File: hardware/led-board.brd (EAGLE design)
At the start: 100 x 15.3 mm, 22 parts, among them U1 ATMEGA168PA-AU

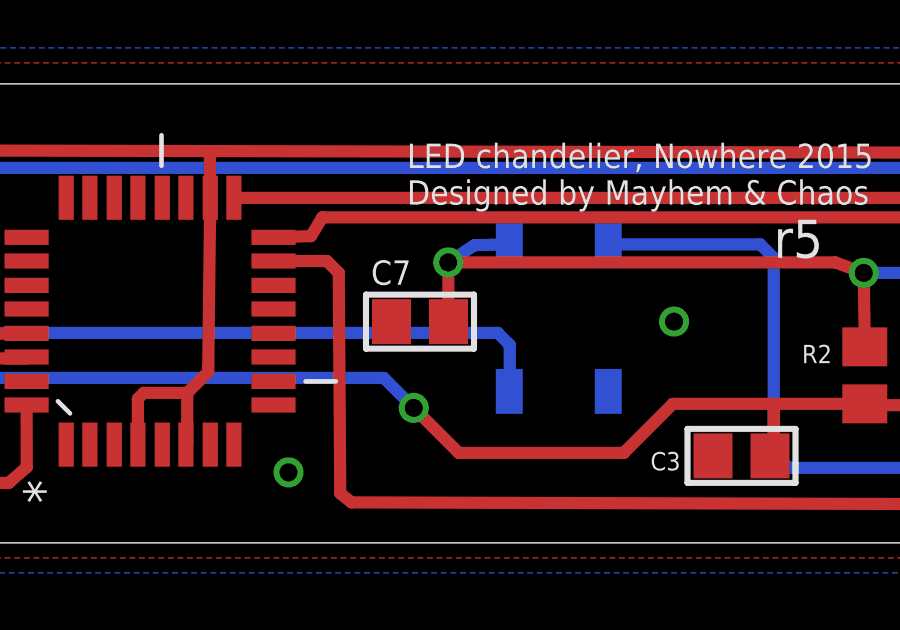
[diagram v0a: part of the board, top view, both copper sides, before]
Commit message: Moved C7 further away from U1
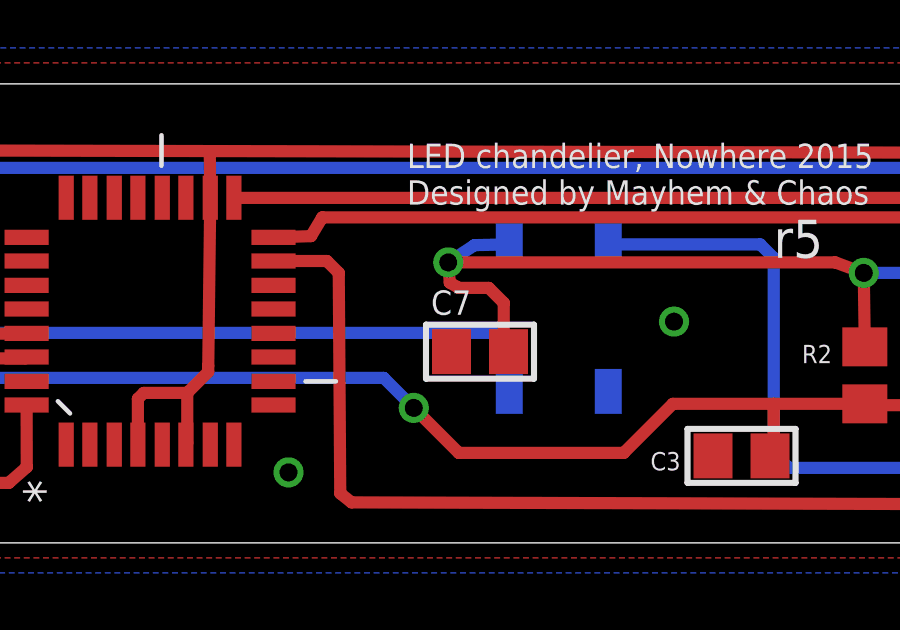
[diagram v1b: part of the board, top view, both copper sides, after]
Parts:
- moved C7 2.24 mm to (62.7, 6.38)
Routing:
- net VCC: track 183.6 -> 186.1 mm
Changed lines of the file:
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@@
 <attribute name="MPN" value="MCSH21B104K250CT" x="39.12" y="7.48" size="1.778" layer="27" rot="R270" display="off"/>
 </element>
-<element name="C7" library="microbuilder" package="0805" value="100nF" x="60.708" y="7.375" smashed="yes" rot="R180">
-<attribute name="NAME" x="59.076" y="8.602" size="0.8128" layer="25" ratio="18"/>
-<attribute name="OC_NEWARK" value="23T7445" x="60.708" y="7.375" size="1.778" layer="27" rot="R180" display="off"/>
-<attribute name="MF" value="" x="60.708" y="7.375" size="1.778" layer="27" rot="R180" display="off"/>
-<attribute name="MPN" value="MCSH21B104K250CT" x="60.708" y="7.375" size="1.778" layer="27" rot="R180" display="off"/>
+<element name="C7" library="microbuilder" package="0805" value="100nF" x="62.708" y="6.375" smashed="yes" rot="R180">
+<attribute name="NAME" x="61.076" y="7.602" size="0.8128" layer="25" ratio="18"/>
+<attribute name="OC_NEWARK" value="23T7445" x="62.708" y="6.375" size="1.778" layer="27" rot="R180" display="off"/>
+<attribute name="MF" value="" x="62.708" y="6.375" size="1.778" layer="27" rot="R180" display="off"/>
+<attribute name="MPN" value="MCSH21B104K250CT" x="62.708" y="6.375" size="1.778" layer="27" rot="R180" display="off"/>
 </element>
 <element name="C8" library="microbuilder" package="0805" value="100nF" x="90.92" y="8.58" smashed="yes" rot="R90">
@@
 <wire x1="85.075" y1="9.7" x2="85.55" y2="9.225" width="0.4064" layer="1"/>
 <wire x1="85.55" y1="9.225" x2="85.55" y2="8.4" width="0.4064" layer="1"/>
-<wire x1="61.658" y1="7.375" x2="61.65" y2="9.35" width="0.4064" layer="1"/>
 <via x="61.65" y="9.35" extent="1-16" drill="0.6"/>
 <wire x1="61.65" y1="9.35" x2="62.525" y2="9.925" width="0.4064" layer="16"/>
@@
 <wire x1="61.65" y1="9.35" x2="74.55" y2="9.35" width="0.4064" layer="1"/>
 <wire x1="74.55" y1="9.35" x2="75.5" y2="9" width="0.4064" layer="1"/>
+<wire x1="63.658" y1="6.375" x2="63.5" y2="6.375" width="0.4064" layer="1"/>
+<wire x1="63.5" y1="6.375" x2="63.5" y2="8" width="0.4064" layer="1"/>
+<wire x1="63.5" y1="8" x2="63" y2="8.5" width="0.4064" layer="1"/>
+<wire x1="63" y1="8.5" x2="62" y2="8.5" width="0.4064" layer="1"/>
+<wire x1="62" y1="8.5" x2="61.7" y2="8.675" width="0.4064" layer="1"/>
+<wire x1="61.7" y1="8.675" x2="61.65" y2="9.35" width="0.4064" layer="1"/>
 </signal>
 <signal name="LED">

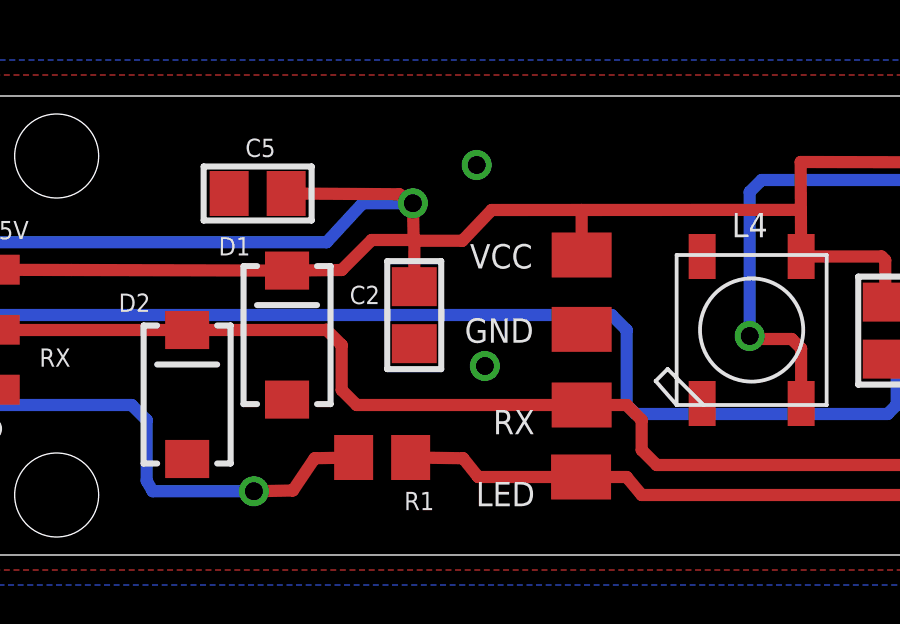
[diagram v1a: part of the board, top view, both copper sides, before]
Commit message: Increased bulk capacitance (C1) to 47uF.
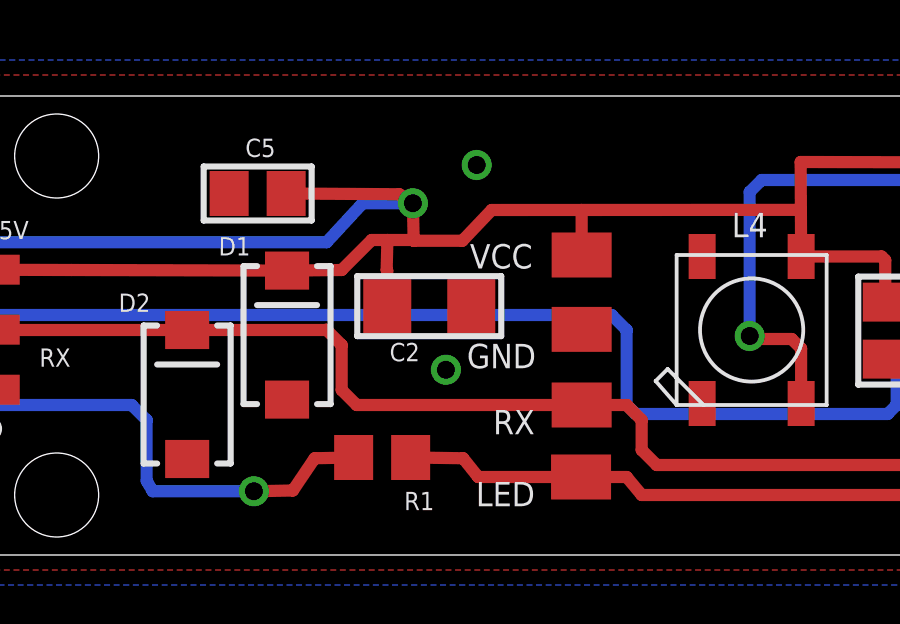
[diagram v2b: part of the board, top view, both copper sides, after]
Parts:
- C2: value 1uF -> 47uF; device microbuilder:0805 -> microbuilder:1206
- moved C2 0.58 mm to (23.9, 8.29), turned to 0 degrees
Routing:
- net VCC: track 186.1 -> 186.8 mm
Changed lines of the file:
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@@
 <wire x1="100" y1="15.3" x2="0" y2="15.3" width="0" layer="20"/>
 <wire x1="0" y1="15.3" x2="0" y2="0" width="0" layer="20"/>
-<text x="25.1" y="7.075" size="0.8128" layer="25">GND</text>
+<text x="25.175" y="6.225" size="0.8128" layer="25">GND</text>
 <text x="26.05" y="4.025" size="0.8128" layer="25">RX</text>
 <text x="25.475" y="1.625" size="0.8128" layer="25">LED</text>
@@
 <attribute name="MPN" value="MCSH21B104K250CT" x="43.02" y="10.98" size="1.778" layer="27" rot="R180" display="off"/>
 </element>
-<element name="C2" library="microbuilder" package="0805" value="1uF" x="23.42" y="7.995" smashed="yes" rot="R270">
-<attribute name="NAME" x="21.268" y="8.363" size="0.6096" layer="25" ratio="18"/>
-<attribute name="OC_NEWARK" value="68R4880" x="23.42" y="7.995" size="1.778" layer="27" rot="R270" display="off"/>
-<attribute name="MF" value="" x="23.42" y="7.995" size="1.778" layer="27" rot="R270" display="off"/>
-<attribute name="MPN" value="CC0805KKX7R7BB105" x="23.42" y="7.995" size="1.778" layer="27" rot="R270" display="off"/>
+<element name="C2" library="microbuilder" package="1206" value="47uF" x="23.92" y="8.295" smashed="yes">
+<attribute name="NAME" x="23.602" y="7.068" size="0.6096" layer="25" ratio="18" rot="R180"/>
+<attribute name="OC_NEWARK" value="68R4880" x="23.92" y="8.295" size="1.778" layer="27" display="off"/>
+<attribute name="MF" value="" x="23.92" y="8.295" size="1.778" layer="27" display="off"/>
+<attribute name="MPN" value="CC0805KKX7R7BB105" x="23.92" y="8.295" size="1.778" layer="27" display="off"/>
 </element>
 <element name="C5" library="microbuilder" package="0805" value="100nF" x="18.2" y="12.05" smashed="yes" rot="R180">
@@
 <contactref element="U1" pad="21"/>
 <contactref element="C3" pad="2"/>
-<via x="25.775" y="6.3" extent="1-16" drill="0.6"/>
+<via x="24.475" y="6.175" extent="1-16" drill="0.6"/>
 <contactref element="D2" pad="A"/>
 <contactref element="D1" pad="A"/>
@@
 <wire x1="19.18" y1="9.48" x2="21" y2="9.5" width="0.4064" layer="1"/>
 <wire x1="21" y1="9.5" x2="22" y2="10.5" width="0.4064" layer="1"/>
-<wire x1="22" y1="10.5" x2="23.425" y2="10.5" width="0.4064" layer="1"/>
+<wire x1="22" y1="10.5" x2="22.525" y2="10.5" width="0.4064" layer="1"/>
+<wire x1="22.525" y1="10.5" x2="23.425" y2="10.5" width="0.4064" layer="1"/>
 <wire x1="23.425" y1="10.5" x2="23.4" y2="10.475" width="0.4064" layer="1"/>
 <wire x1="23.4" y1="10.475" x2="25.025" y2="10.475" width="0.4064" layer="1"/>
 <wire x1="25.025" y1="10.475" x2="26" y2="11.5" width="0.4064" layer="1"/>
-<wire x1="23.42" y1="8.945" x2="23.425" y2="10.5" width="0.4064" layer="1"/>
 <wire x1="26" y1="11.5" x2="28.9998" y2="11.50119375" width="0.4064" layer="1"/>
 <wire x1="28.9998" y1="11.50119375" x2="36.30810625" y2="11.504103125" width="0.4064" layer="1"/>
@@
 <wire x1="62" y1="8.5" x2="61.7" y2="8.675" width="0.4064" layer="1"/>
 <wire x1="61.7" y1="8.675" x2="61.65" y2="9.35" width="0.4064" layer="1"/>
+<wire x1="22.52" y1="8.295" x2="22.52" y2="9.48" width="0.4064" layer="1"/>
+<wire x1="22.52" y1="9.48" x2="22.5" y2="9.5" width="0.4064" layer="1"/>
+<wire x1="22.5" y1="9.5" x2="22.525" y2="10.5" width="0.4064" layer="1"/>
 </signal>
 <signal name="LED">

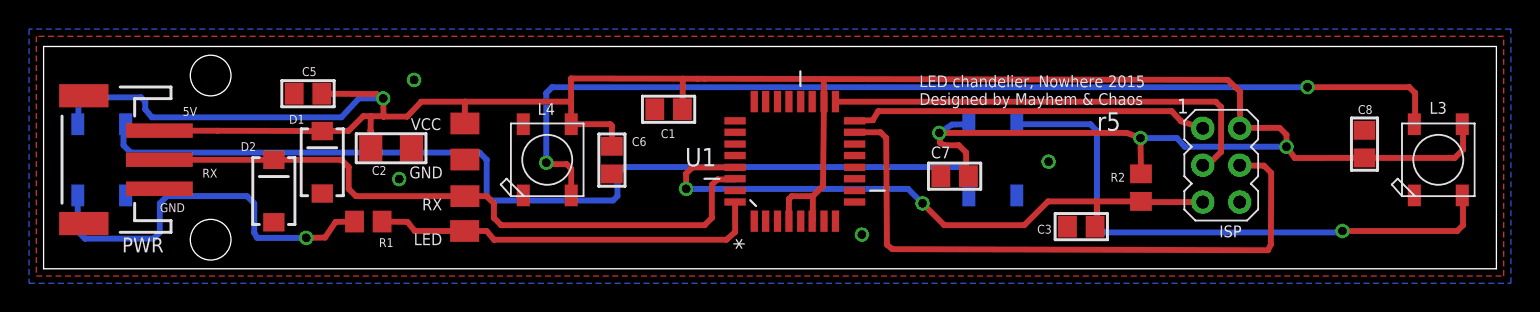
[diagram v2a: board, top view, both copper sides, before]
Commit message: Changed L# -> D# for the LEDs
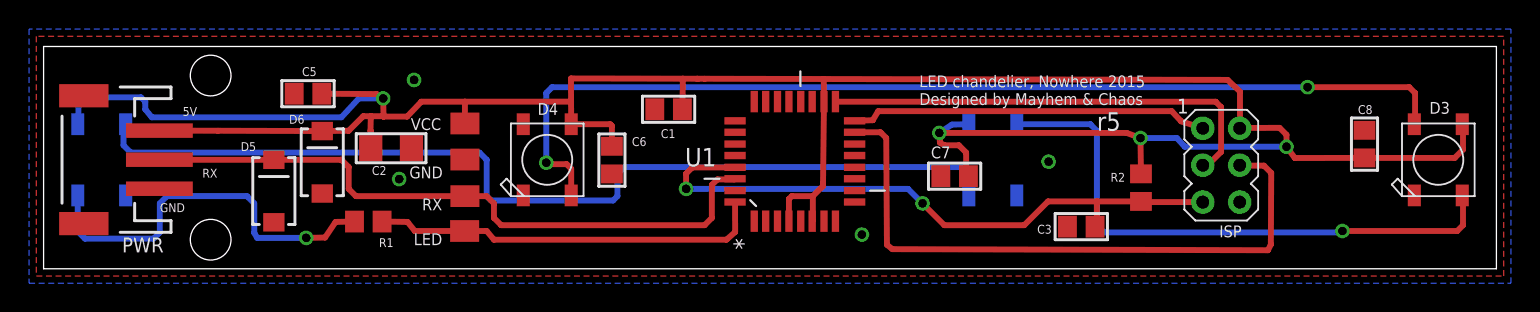
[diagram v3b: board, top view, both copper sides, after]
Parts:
- removed L1, L2: WS2812B, adafruit:WS2812B
- added D5, D6: BA340A, SparkFun-DiscreteSemi:SMA-DIODE
- D1, D2: value BA340A -> WS2812B; device SparkFun-DiscreteSemi:SMA-DIODE -> adafruit:WS2812B
- moved D2 49.5 mm to (65.3, 7.50), flipped to the bottom
- moved D1 15.2 mm to (4.00, 7.50), flipped to the bottom
- renumbered L3 to D3, L4 to D4
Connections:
- removed net N$5: D3.4-DIN, L2.2-DOUT
- new net D3: D2.2-DOUT, D3.4-DIN
- net GND: now also D1.3-GND, D2.3-GND, D5.A, D6.A; no longer D1.A, D2.A, L1.3-GND, L2.3-GND
- net N$2: now also D1.2-DOUT, D2.4-DIN; no longer L1.2-DOUT, L2.4-DIN
- net N$8: now also D1.4-DIN; no longer L1.4-DIN
- net RX: now also D5.C; no longer D2.C
- net VCC: now also D1.1-VDD, D2.1-VDD, D6.C; no longer D1.C, L1.1-VDD, L2.1-VDD
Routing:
- net N$5: track 39.9 -> 0.00 mm, vias 1 -> 0
- net D3: track 0.00 -> 39.9 mm, vias 0 -> 1
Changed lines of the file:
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@@
 <attribute name="MPN" value="MCSH21B104K250CT" x="90.92" y="8.58" size="1.778" layer="27" rot="R90" display="off"/>
 </element>
-<element name="D1" library="SparkFun-DiscreteSemi" package="SMA-DIODE" value="BA340A" x="19.18" y="7.33" smashed="yes" rot="R90">
+<element name="D6" library="SparkFun-DiscreteSemi" package="SMA-DIODE" value="BA340A" x="19.18" y="7.33" smashed="yes" rot="R90">
 <attribute name="PROD_ID" value="DIO-09886" x="19.18" y="7.33" size="1.778" layer="27" rot="R90" display="off"/>
 <attribute name="NAME" x="17.954" y="10.594" size="0.6096" layer="25" rot="R180"/>
@@
 <attribute name="MPN" value="" x="81.06" y="7.13" size="1.778" layer="27" display="off"/>
 </element>
-<element name="L1" library="adafruit" package="WS2812B" value="WS2812B" x="4" y="7.5" smashed="yes" rot="MR90">
+<element name="D1" library="adafruit" package="WS2812B" value="WS2812B" x="4" y="7.5" smashed="yes" rot="MR90">
 <attribute name="NAME" x="4.5125" y="10.3425" size="0.8128" layer="26" ratio="10" rot="MR0"/>
 <attribute name="OC_NEWARK" value="43Y4720" x="4" y="7.5" size="1.778" layer="28" rot="MR90" display="off"/>
@@
 <attribute name="MPN" value="WS2812B" x="4" y="7.5" size="1.778" layer="28" rot="MR90" display="off"/>
 </element>
-<element name="L2" library="adafruit" package="WS2812B" value="WS2812B" x="65.333" y="7.5" smashed="yes" rot="MR90">
+<element name="D2" library="adafruit" package="WS2812B" value="WS2812B" x="65.333" y="7.5" smashed="yes" rot="MR90">
 <attribute name="NAME" x="65.8705" y="10.6675" size="0.8128" layer="26" ratio="10" rot="MR0"/>
 <attribute name="OC_NEWARK" value="43Y4720" x="65.333" y="7.5" size="1.778" layer="28" rot="MR90" display="off"/>
@@
 <attribute name="MPN" value="WS2812B" x="65.333" y="7.5" size="1.778" layer="28" rot="MR90" display="off"/>
 </element>
-<element name="L3" library="adafruit" package="WS2812B" value="WS2812B" x="96" y="7.5" smashed="yes" rot="R90">
+<element name="D3" library="adafruit" package="WS2812B" value="WS2812B" x="96" y="7.5" smashed="yes" rot="R90">
 <attribute name="NAME" x="95.3875" y="10.6675" size="0.8128" layer="25" ratio="10"/>
 <attribute name="OC_NEWARK" value="43Y4720" x="96" y="7.5" size="1.778" layer="27" rot="R90" display="off"/>
@@
 <attribute name="MPN" value="WS2812B" x="96" y="7.5" size="1.778" layer="27" rot="R90" display="off"/>
 </element>
-<element name="L4" library="adafruit" package="WS2812B" value="WS2812B" x="34.666" y="7.5" smashed="yes" rot="R90">
+<element name="D4" library="adafruit" package="WS2812B" value="WS2812B" x="34.666" y="7.5" smashed="yes" rot="R90">
 <attribute name="NAME" x="34.0035" y="10.5925" size="0.8128" layer="25" ratio="10"/>
 <attribute name="OC_NEWARK" value="43Y4720" x="34.666" y="7.5" size="1.778" layer="27" rot="R90" display="off"/>
@@
 <attribute name="MF" value="" x="51.71" y="7.39" size="1.778" layer="27" rot="R90" display="off"/>
 </element>
-<element name="D2" library="SparkFun-DiscreteSemi" package="SMA-DIODE" value="BA340A" x="15.85" y="5.35" smashed="yes" rot="R90">
+<element name="D5" library="SparkFun-DiscreteSemi" package="SMA-DIODE" value="BA340A" x="15.85" y="5.35" smashed="yes" rot="R90">
 <attribute name="PROD_ID" value="DIO-09886" x="15.85" y="5.35" size="1.778" layer="27" rot="R90" display="off"/>
 <attribute name="NAME" x="14.624" y="8.714" size="0.6096" layer="25" rot="R180"/>
@@
 <contactref element="ISP" pad="6"/>
 <contactref element="TP_GND" pad="P$1"/>
-<contactref element="L1" pad="3-GND"/>
-<contactref element="L3" pad="3-GND"/>
+<contactref element="D1" pad="3-GND"/>
+<contactref element="D3" pad="3-GND"/>
 <contactref element="C8" pad="2"/>
-<contactref element="L4" pad="3-GND"/>
+<contactref element="D4" pad="3-GND"/>
 <contactref element="C6" pad="2"/>
-<contactref element="L2" pad="3-GND"/>
+<contactref element="D2" pad="3-GND"/>
 <contactref element="C5" pad="2"/>
 <contactref element="C7" pad="2"/>
@@
 <contactref element="C3" pad="2"/>
 <via x="24.475" y="6.175" extent="1-16" drill="0.6"/>
-<contactref element="D2" pad="A"/>
-<contactref element="D1" pad="A"/>
+<contactref element="D5" pad="A"/>
+<contactref element="D6" pad="A"/>
 <via x="56.325" y="2.35" extent="1-16" drill="0.6"/>
 <via x="25.5" y="13" extent="1-16" drill="0.6"/>
@@
 </signal>
 <signal name="N$2">
-<contactref element="L1" pad="2-DOUT"/>
-<contactref element="L2" pad="4-DIN"/>
+<contactref element="D1" pad="2-DOUT"/>
+<contactref element="D2" pad="4-DIN"/>
 <wire x1="39.2" y1="4.7" x2="39.5" y2="5" width="0.4064" layer="16"/>
 <wire x1="39.5" y1="5" x2="39.5" y2="6.5" width="0.4064" layer="16"/>
@@
 </signal>
 <signal name="N$1">
-<contactref element="L3" pad="2-DOUT"/>
-<contactref element="L4" pad="4-DIN"/>
+<contactref element="D3" pad="2-DOUT"/>
+<contactref element="D4" pad="4-DIN"/>
 <wire x1="36.316" y1="5.05" x2="36.316" y2="6.884" width="0.4064" layer="1"/>
 <wire x1="36.316" y1="6.884" x2="36" y2="7.2" width="0.4064" layer="1"/>
@@
 <wire x1="47.5866" y1="6.975" x2="47.5952" y2="6.9836" width="0.4064" layer="1"/>
 </signal>
-<signal name="N$5">
-<contactref element="L2" pad="2-DOUT"/>
-<contactref element="L3" pad="4-DIN"/>
+<signal name="D3">
+<contactref element="D2" pad="2-DOUT"/>
+<contactref element="D3" pad="4-DIN"/>
 <wire x1="66.983" y1="9.95" x2="72.05" y2="9.95" width="0.4064" layer="16"/>
 <wire x1="73" y1="2.5" x2="89.3" y2="2.5" width="0.4064" layer="16"/>
@@
 <signal name="N$8">
 <contactref element="R1" pad="2"/>
-<contactref element="L1" pad="4-DIN"/>
+<contactref element="D1" pad="4-DIN"/>
 <via x="18.075" y="2.125" extent="1-16" drill="0.6"/>
 <wire x1="2.85" y1="2.075" x2="2.35" y2="2.575" width="0.4064" layer="16"/>
@@
 <contactref element="ISP" pad="2"/>
 <contactref element="C8" pad="1"/>
-<contactref element="L1" pad="1-VDD"/>
+<contactref element="D1" pad="1-VDD"/>
 <contactref element="C7" pad="1"/>
 <contactref element="C6" pad="1"/>
-<contactref element="L4" pad="1-VDD"/>
+<contactref element="D4" pad="1-VDD"/>
 <contactref element="C5" pad="1"/>
-<contactref element="L2" pad="1-VDD"/>
-<contactref element="L3" pad="1-VDD"/>
+<contactref element="D2" pad="1-VDD"/>
+<contactref element="D3" pad="1-VDD"/>
 <contactref element="S2B-PH-SM4" pad="3"/>
 <contactref element="C2" pad="1"/>
@@
 <wire x1="39.12" y1="8.43" x2="39.12" y2="9.83" width="0.4064" layer="1"/>
 <wire x1="39.12" y1="9.83" x2="39" y2="9.95" width="0.4064" layer="1"/>
-<contactref element="D1" pad="C"/>
+<contactref element="D6" pad="C"/>
 <wire x1="19.18" y1="9.48" x2="12" y2="9.5" width="0.4064" layer="1"/>
 <contactref element="TP_RX1" pad="P$1"/>
@@
 <wire x1="20.48" y1="7.5" x2="20.49" y2="7.51" width="0.4064" layer="1"/>
 <wire x1="8.28" y1="7.5" x2="7.97" y2="7.51" width="0.4064" layer="1"/>
-<contactref element="D2" pad="C"/>
+<contactref element="D5" pad="C"/>
 <wire x1="8.28" y1="7.5" x2="15.85" y2="7.5" width="0.4064" layer="1"/>
 <wire x1="15.85" y1="7.5" x2="20.48" y2="7.5" width="0.4064" layer="1"/>
